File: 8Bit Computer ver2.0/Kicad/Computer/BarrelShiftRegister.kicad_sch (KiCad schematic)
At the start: 6 parts, among them IC75 SN74AHC157DR, IC76 SN74AHC157DR, IC77 SN74AHC157DR, IC78 SN74AHC157DR, IC79 SN74AHC157DR, IC80 SN74AHC157DR

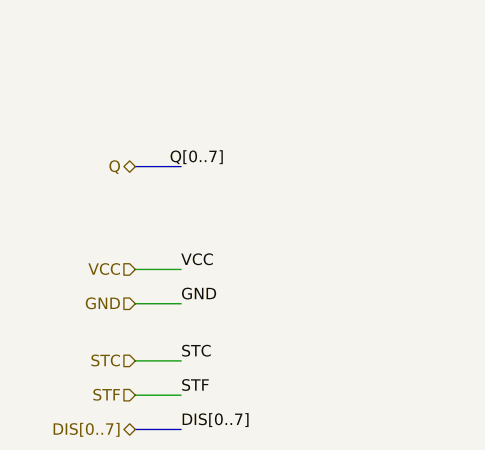
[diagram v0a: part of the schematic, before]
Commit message: partsList, Kicad
parts:
added faster Comparator 521
added 1CH XOR
added 8Bit and 16Bit Driver 245, 16245
->they need pullUp resistors for High-Z when power on
Kicad:
included SRAM CAD Model AS7C1024
included some CAD Models
added Register 1 0x20 and 0x21
finished Incrementor
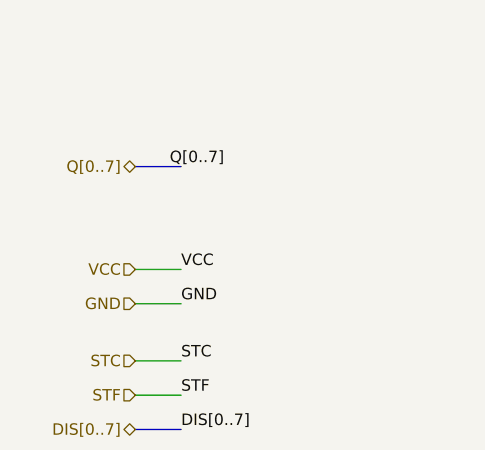
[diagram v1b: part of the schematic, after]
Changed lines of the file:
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@@
 		)
 	)
-	(hierarchical_label "Q"
+	(hierarchical_label "Q[0..7]"
 		(shape tri_state)
 		(at 39.37 43.18 180)

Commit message: Kicad
added Register 2(0x22 u 0x23) and 3(0x13 u 0x14)
added BarrelShiftRegister
added AdderSubstractor
added cmd Comparators to the bitwise and binary Logic
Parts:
- added IC115, IC116, IC117: SN74LVC1G08DBVR, Samacsys:SOT95P280X145-5N, symbol Samacsys:SN74LVC1G08DBVR
- added IC118: SN74AHC08DR, Samacsys:SOIC127P600X175-14N, symbol Samacsys:SN74AHC08DR
- added IC119: SN74ABT574ADWR, Samacsys:SOIC127P1030X265-20N, symbol Samacsys:SN74ABT574ADWR
- added IC120: SN74LVC1G32DBVR, Samacsys:SOT95P280X145-5N, symbol Samacsys:SN74LVC1G32DBVR
- added IC121: SN74AHC74DR, Samacsys:SOIC127P600X175-14N, symbol Samacsys:SN74AHC74DR
- added IC122: SN74LVC1G14DBVR, Samacsys:SOT95P280X145-5N, symbol Samacsys:SN74LVC1G14DBVR
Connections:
- net GND: now also IC115.3 (GND), IC116.3 (GND), IC117.3 (GND), IC118.7 (GND), IC119.10 (GND), IC120.3 (GND), IC121.7 (GND), IC122.3 (GND)
- net STC: now also IC115.2 (B), IC116.2 (B), IC117.2 (B), IC118.12 (4A), IC118.2 (1B), IC118.5 (2B), IC118.9 (3A)
- net VCC: now also IC115.5 (VCC), IC116.5 (VCC), IC117.5 (VCC), IC118.14 (VCC), IC119.20 (VCC), IC120.5 (VCC), IC121.1 (1~{CLR}), IC121.10 (2~{PRE}), IC121.11 (2CLK), IC121.12 (2D), IC121.13 (2~{CLR}), IC121.14 (VCC), IC121.4 (1~{PRE}), IC122.5 (VCC)
- net ~{CLK}: now also IC122.2 (A)
- net DIS1: now reaches IC77.1 (~{A}/B)
- net DIS1: now also IC78.1 (~{A}/B)
- net STC1Stage1: now reaches IC77.10 (3B)
- net STC1Stage1: now also IC117.4 (Y)
- net 1Stage7: now reaches IC77.11 (3A)
- net 1Stage7: now also IC76.9 (3Y), IC78.10 (3B)
- net 2Stage6: now reaches IC77.12 (4Y)
- net 2Stage6: now also IC80.14 (4A), IC80.3 (1B)
- net STC1Stage0: now reaches IC77.13 (4B)
- net STC1Stage0: now also IC116.4 (Y)
- net 1Stage6: now reaches IC77.14 (4A)
- net 1Stage6: now also IC76.12 (4Y), IC78.13 (4B)
- net 1Stage2: now reaches IC77.2 (1A)
- net 1Stage2: now also IC76.4 (1Y), IC78.3 (1B)
- net 1Stage4: now reaches IC77.3 (1B)
- net 1Stage4: now also IC75.12 (4Y), IC78.14 (4A)
- net 2Stage2: now reaches IC77.4 (1Y)
- net 2Stage2: now also IC80.2 (1A), IC118.13 (4B)
- net 1Stage3: now reaches IC77.5 (2A)
- net 1Stage3: now also IC76.7 (2Y), IC78.6 (2B)
- net 1Stage5: now reaches IC77.6 (2B)
- net 1Stage5: now also IC75.9 (3Y), IC78.11 (3A)
- net 2Stage3: now reaches IC77.7 (2Y)
- net 2Stage3: now also IC80.5 (2A), IC118.10 (3B)
- net 2Stage7: now reaches IC77.9 (3Y)
- net 2Stage7: now also IC80.11 (3A), IC80.6 (2B)
- net DIS0: now reaches IC76.1 (~{A}/B)
- net DIS0: now also IC75.1 (~{A}/B)
- net STCA0: now reaches IC76.10 (3B)
- net STCA0: now also IC115.4 (Y)
- net A7: now reaches IC76.11 (3A)
- net A7: now also IC76.13 (4B)
- net A6: now reaches IC76.14 (4A)
- net A6: now also IC75.10 (3B)
- net A2: now reaches IC76.2 (1A)
- net A2: now also IC75.6 (2B)
- net A3: now reaches IC76.3 (1B)
- net A3: now also IC76.5 (2A)
- net A4: now reaches IC76.6 (2B)
- net A4: now also IC75.14 (4A)
- net DIS2: now reaches IC79.1 (~{A}/B)
- net DIS2: now also IC80.1 (~{A}/B)
- net STC2Stage1: now reaches IC79.10 (3B)
- net STC2Stage1: now also IC118.6 (2Y)
- net 2Stage5: now reaches IC79.11 (3A)
- net 2Stage5: now also IC78.9 (3Y), IC79.6 (2B)
- net 3Stage4: now reaches IC79.12 (4Y)
- net 3Stage4: now also IC119.6 (5D)
- net STC2Stage0: now reaches IC79.13 (4B)
- net STC2Stage0: now also IC118.3 (1Y)
- net 2Stage4: now reaches IC79.14 (4A)
- net 2Stage4: now also IC78.12 (4Y), IC79.3 (1B)
- net 2Stage0: now reaches IC79.2 (1A)
- net 2Stage0: now also IC78.4 (1Y), IC118.1 (1A)
- net 3Stage0: now reaches IC79.4 (1Y)
- net 3Stage0: now also IC119.2 (1D)
- net 2Stage1: now reaches IC79.5 (2A)
- net 2Stage1: now also IC78.7 (2Y), IC118.4 (2A)
- net 3Stage1: now reaches IC79.7 (2Y)
- net 3Stage1: now also IC119.3 (2D)
- net 3Stage5: now reaches IC79.9 (3Y)
- net 3Stage5: now also IC119.7 (6D)
- net STC2Stage3: now reaches IC80.10 (3B)
- net STC2Stage3: now also IC118.8 (3Y)
- net 3Stage6: now reaches IC80.12 (4Y)
- net 3Stage6: now also IC119.8 (7D)
- net STC2Stage2: now reaches IC80.13 (4B)
- net STC2Stage2: now also IC118.11 (4Y)
- net 3Stage2: now reaches IC80.4 (1Y)
- net 3Stage2: now also IC119.4 (3D)
- net 3Stage3: now reaches IC80.7 (2Y)
- net 3Stage3: now also IC119.5 (4D)
- net 3Stage7: now reaches IC80.9 (3Y)
- net 3Stage7: now also IC119.9 (8D)
- net 1Stage0: now reaches IC78.2 (1A)
- net 1Stage0: now also IC75.4 (1Y), IC116.1 (A)
- net 1Stage1: now reaches IC78.5 (2A)
- net 1Stage1: now also IC75.7 (2Y), IC117.1 (A)
- net A5: now reaches IC75.11 (3A)
- net A5: now also IC75.13 (4B)
- net A0: now reaches IC75.2 (1A)
- net A0: now also IC115.1 (A)
- net A1: now reaches IC75.3 (1B)
- net A1: now also IC75.5 (2A)
- new net: IC119.1 (~{OE}), IC121.6 (1~{Q})
- new net: IC119.11 (CLK), IC121.5 (1Q)
- new net: IC121.3 (1CLK), IC122.4 (Y)
- new net: IC120.4 (Y), IC121.2 (1D)
- new net Q0: IC119.19 (1Q)
- new net Q1: IC119.18 (2Q)
- new net Q2: IC119.17 (3Q)
- new net Q3: IC119.16 (4Q)
- new net Q4: IC119.15 (5Q)
- new net Q5: IC119.14 (6Q)
- new net Q6: IC119.13 (7Q)
- new net Q7: IC119.12 (8Q)
- new net SFC: IC120.2 (B)
- new net SFT: IC120.1 (A)
- no-connect marks 0 -> 2
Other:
- moved on the sheet: IC75, IC76, IC77, IC78, IC79, IC80

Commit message: Kicad, parts
Parts:
added Leds
Kicad:
added Input Output
changed Q bus to DAT bus
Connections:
- net Q0 renamed DAT0
- net Q1 renamed DAT1
- net Q2 renamed DAT2
- net Q3 renamed DAT3
- net Q4 renamed DAT4
- net Q5 renamed DAT5
- net Q6 renamed DAT6
- net Q7 renamed DAT7
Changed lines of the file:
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@@
 		)
 	)
-	(label "Q6"
+	(label "DAT6"
 		(at 400.05 129.54 0)
 		(effects
@@
 		)
 	)
-	(label "Q5"
+	(label "DAT5"
 		(at 400.05 127 0)
 		(effects
@@
 		)
 	)
-	(label "Q7"
+	(label "DAT7"
 		(at 400.05 132.08 0)
 		(effects
@@
 		)
 	)
-	(label "Q4"
+	(label "DAT4"
 		(at 400.05 124.46 0)
 		(effects
@@
 		)
 	)
-	(label "Q3"
+	(label "DAT3"
 		(at 400.05 121.92 0)
 		(effects
@@
 		)
 	)
-	(label "Q[0..7]"
+	(label "DAT[0..7]"
 		(at 40.64 80.01 0)
 		(effects
@@
 		)
 	)
-	(label "Q0"
+	(label "DAT0"
 		(at 400.05 114.3 0)
 		(effects
@@
 		)
 	)
-	(label "Q2"
+	(label "DAT2"
 		(at 400.05 119.38 0)
 		(effects
@@
 		)
 	)
-	(label "Q[0..7]"
+	(label "DAT[0..7]"
 		(at 411.48 104.14 0)
 		(effects
@@
 		)
 	)
-	(label "Q1"
+	(label "DAT1"
 		(at 400.05 116.84 0)
 		(effects
@@
 		)
 	)
-	(hierarchical_label "Q[0..7]"
+	(hierarchical_label "DAT[0..7]"
 		(shape tri_state)
 		(at 36.83 80.01 180)

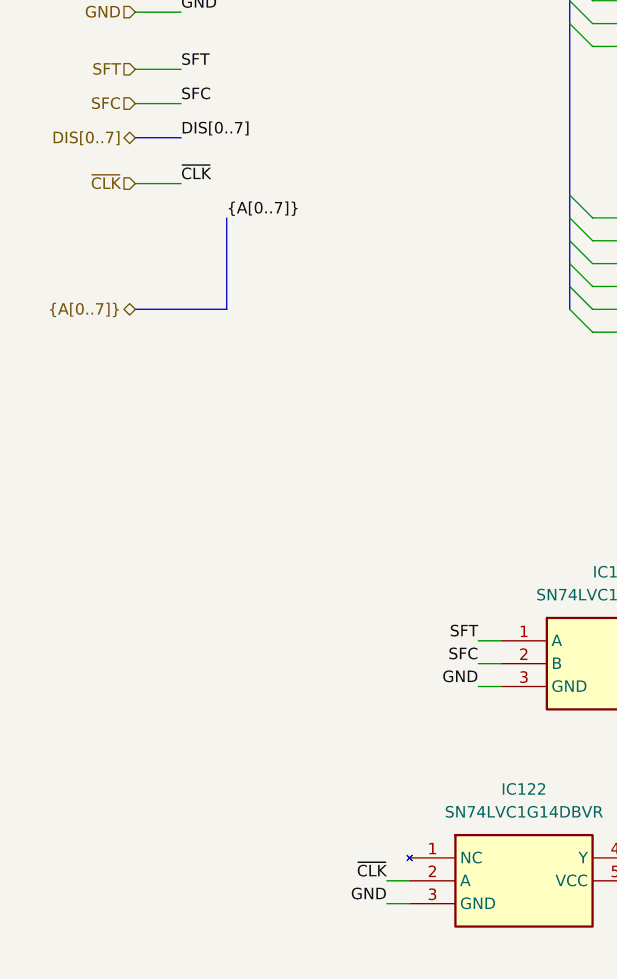
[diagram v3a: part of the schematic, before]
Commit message: Kicad, parts
parts:
added USB C PD Triggerboard
added Delay Chip for 90ns
added Push Button
Kicad:
added USB C PD Triggerboard
added rising edge detector via Delay and Xor for Accept Push Button
added VBUS net
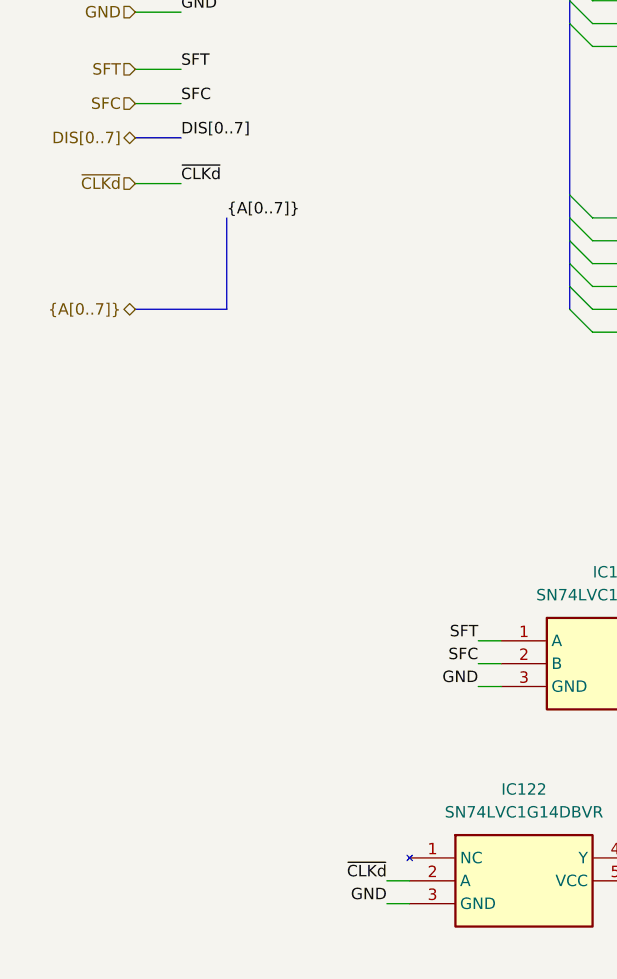
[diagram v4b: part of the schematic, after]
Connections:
- net ~{CLK} renamed ~{CLKd}
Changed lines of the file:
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@@
 		)
 	)
-	(label "~{CLK}"
+	(label "~{CLKd}"
 		(at 41.91 114.3 0)
 		(effects
@@
 		)
 	)
-	(label "~{CLK}"
+	(label "~{CLKd}"
 		(at 64.77 191.77 180)
 		(effects
@@
 		)
 	)
-	(hierarchical_label "~{CLK}"
+	(hierarchical_label "~{CLKd}"
 		(shape input)
 		(at 36.83 114.3 180)

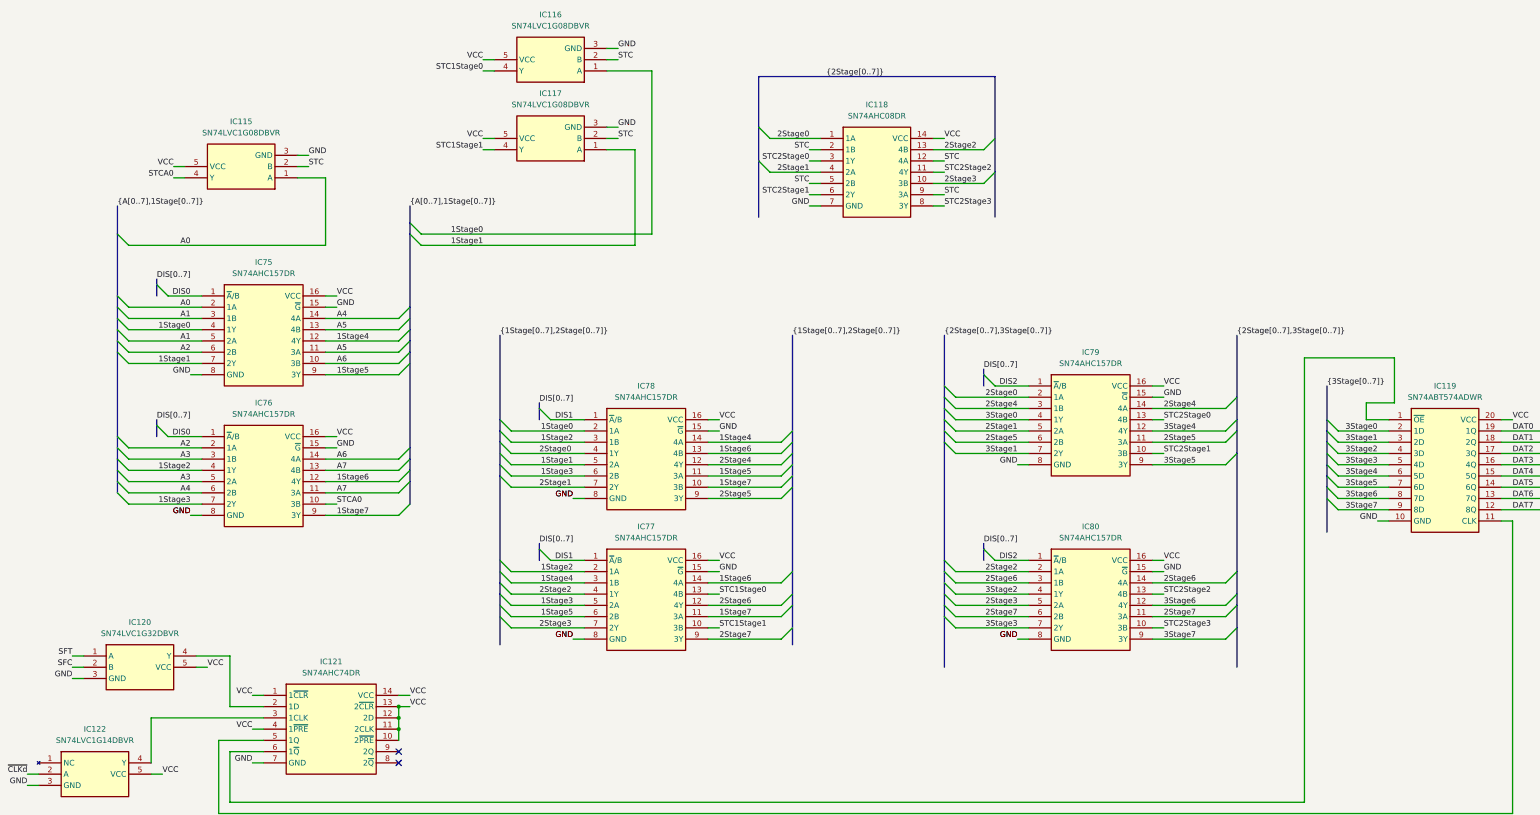
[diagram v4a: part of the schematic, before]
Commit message: Kicad SCH/PCB
Kicad SCH/PCB:
changed the References in SCH
began with INOUTPUT module nearly done
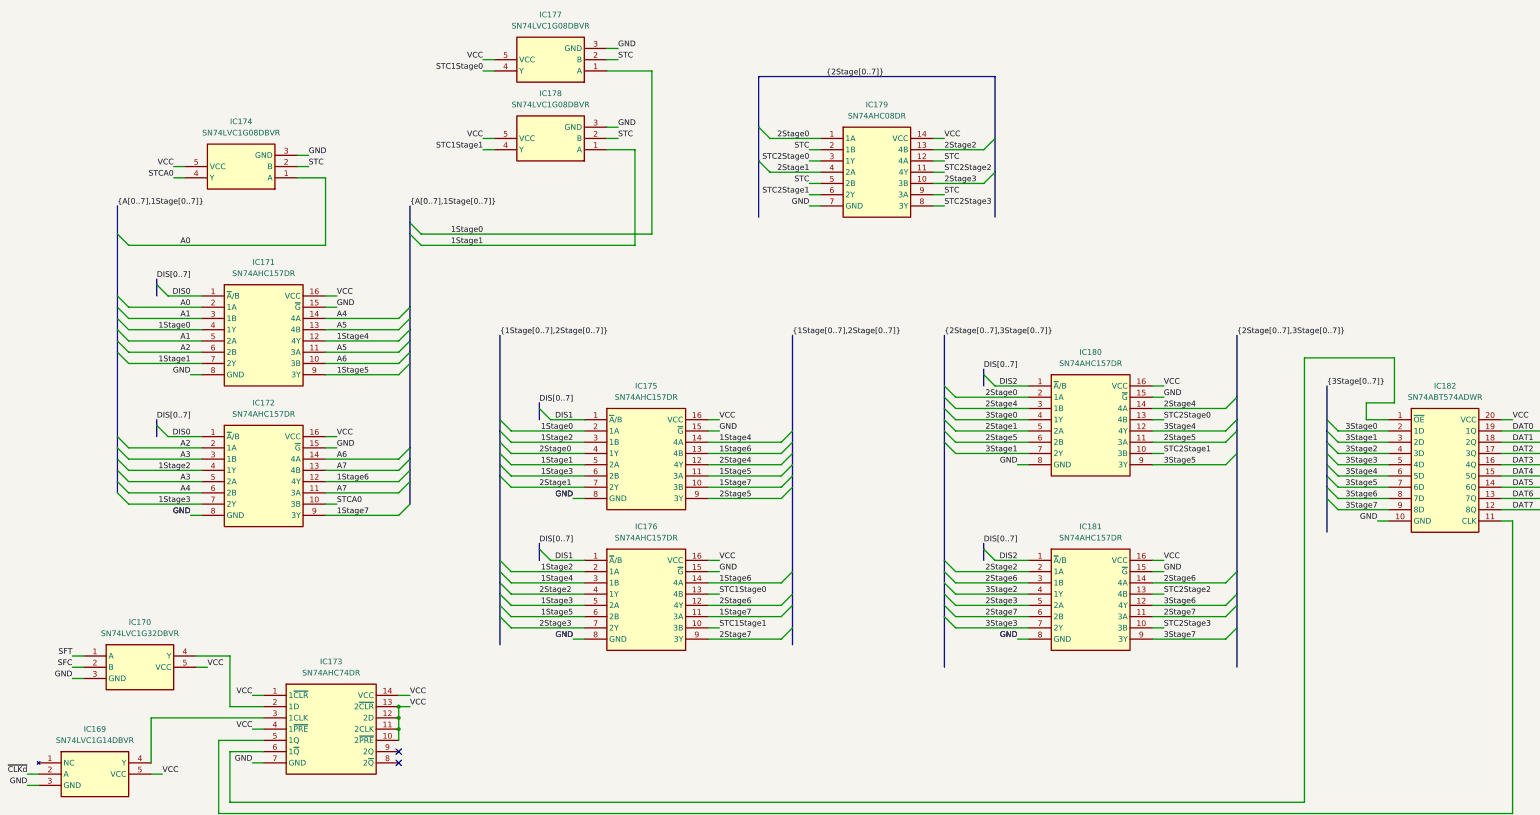
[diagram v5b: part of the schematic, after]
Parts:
- renumbered IC122 to IC169, IC120 to IC170, IC75 to IC171, IC76 to IC172, IC121 to IC173, IC115 to IC174, IC78 to IC175, IC77 to IC176, IC116 to IC177, IC117 to IC178, IC118 to IC179, IC79 to IC180, IC80 to IC181, IC119 to IC182
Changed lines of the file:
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@@
 		(dnp no)
 		(fields_autoplaced yes)
-		(property "Reference" "IC116"
+		(property "Reference" "IC177"
 			(at 182.88 20.32 0)
 			(effects
@@
 			(project "Computer"
 				(path "/1196a00e-6878-4d6d-82b7-9e052dfe7c14/c4d8b530-1c6d-45af-88d2-7dc1d4321a34/94505ca6-4c2b-4b0f-b160-ac9607e51728"
-					(reference "IC116")
+					(reference "IC177")
 					(unit 1)
 				)
@@
 		(dnp no)
 		(fields_autoplaced yes)
-		(property "Reference" "IC77"
+		(property "Reference" "IC176"
 			(at 204.47 135.89 0)
 			(effects
@@
 			(project "Computer"
 				(path "/1196a00e-6878-4d6d-82b7-9e052dfe7c14/c4d8b530-1c6d-45af-88d2-7dc1d4321a34/94505ca6-4c2b-4b0f-b160-ac9607e51728"
-					(reference "IC77")
+					(reference "IC176")
 					(unit 1)
 				)
@@
 		(dnp no)
 		(fields_autoplaced yes)
-		(property "Reference" "IC76"
+		(property "Reference" "IC172"
 			(at 118.11 107.95 0)
 			(effects
@@
 			(project "Computer"
 				(path "/1196a00e-6878-4d6d-82b7-9e052dfe7c14/c4d8b530-1c6d-45af-88d2-7dc1d4321a34/94505ca6-4c2b-4b0f-b160-ac9607e51728"
-					(reference "IC76")
+					(reference "IC172")
 					(unit 1)
 				)
@@
 		(dnp no)
 		(fields_autoplaced yes)
-		(property "Reference" "IC79"
+		(property "Reference" "IC180"
 			(at 304.8 96.52 0)
 			(effects
@@
 			(project "Computer"
 				(path "/1196a00e-6878-4d6d-82b7-9e052dfe7c14/c4d8b530-1c6d-45af-88d2-7dc1d4321a34/94505ca6-4c2b-4b0f-b160-ac9607e51728"
-					(reference "IC79")
+					(reference "IC180")
 					(unit 1)
 				)
@@
 		(dnp no)
 		(fields_autoplaced yes)
-		(property "Reference" "IC80"
+		(property "Reference" "IC181"
 			(at 304.8 135.89 0)
 			(effects
@@
 			(project "Computer"
 				(path "/1196a00e-6878-4d6d-82b7-9e052dfe7c14/c4d8b530-1c6d-45af-88d2-7dc1d4321a34/94505ca6-4c2b-4b0f-b160-ac9607e51728"
-					(reference "IC80")
+					(reference "IC181")
 					(unit 1)
 				)
@@
 		(dnp no)
 		(fields_autoplaced yes)
-		(property "Reference" "IC119"
+		(property "Reference" "IC182"
 			(at 384.81 104.14 0)
 			(effects
@@
 			(project ""
 				(path "/1196a00e-6878-4d6d-82b7-9e052dfe7c14/c4d8b530-1c6d-45af-88d2-7dc1d4321a34/94505ca6-4c2b-4b0f-b160-ac9607e51728"
-					(reference "IC119")
+					(reference "IC182")
 					(unit 1)
 				)
@@
 		(dnp no)
 		(fields_autoplaced yes)
-		(property "Reference" "IC117"
+		(property "Reference" "IC178"
 			(at 182.88 38.1 0)
 			(effects
@@
 			(project "Computer"
 				(path "/1196a00e-6878-4d6d-82b7-9e052dfe7c14/c4d8b530-1c6d-45af-88d2-7dc1d4321a34/94505ca6-4c2b-4b0f-b160-ac9607e51728"
-					(reference "IC117")
+					(reference "IC178")
 					(unit 1)
 				)
@@
 		(dnp no)
 		(fields_autoplaced yes)
-		(property "Reference" "IC118"
+		(property "Reference" "IC179"
 			(at 256.54 40.64 0)
 			(effects
@@
 			(project ""
 				(path "/1196a00e-6878-4d6d-82b7-9e052dfe7c14/c4d8b530-1c6d-45af-88d2-7dc1d4321a34/94505ca6-4c2b-4b0f-b160-ac9607e51728"
-					(reference "IC118")
+					(reference "IC179")
 					(unit 1)
 				)
@@
 		(dnp no)
 		(fields_autoplaced yes)
-		(property "Reference" "IC122"
+		(property "Reference" "IC169"
 			(at 80.01 181.61 0)
 			(effects
@@
 			(project ""
 				(path "/1196a00e-6878-4d6d-82b7-9e052dfe7c14/c4d8b530-1c6d-45af-88d2-7dc1d4321a34/94505ca6-4c2b-4b0f-b160-ac9607e51728"
-					(reference "IC122")
+					(reference "IC169")
 					(unit 1)
 				)
@@
 		(dnp no)
 		(fields_autoplaced yes)
-		(property "Reference" "IC115"
+		(property "Reference" "IC174"
 			(at 113.03 44.45 0)
 			(effects
@@
 			(project ""
 				(path "/1196a00e-6878-4d6d-82b7-9e052dfe7c14/c4d8b530-1c6d-45af-88d2-7dc1d4321a34/94505ca6-4c2b-4b0f-b160-ac9607e51728"
-					(reference "IC115")
+					(reference "IC174")
 					(unit 1)
 				)
@@
 		(dnp no)
 		(fields_autoplaced yes)
-		(property "Reference" "IC120"
+		(property "Reference" "IC170"
 			(at 90.17 157.48 0)
 			(effects
@@
 			(project ""
 				(path "/1196a00e-6878-4d6d-82b7-9e052dfe7c14/c4d8b530-1c6d-45af-88d2-7dc1d4321a34/94505ca6-4c2b-4b0f-b160-ac9607e51728"
-					(reference "IC120")
+					(reference "IC170")
 					(unit 1)
 				)
@@
 		(dnp no)
 		(fields_autoplaced yes)
-		(property "Reference" "IC121"
+		(property "Reference" "IC173"
 			(at 133.35 166.37 0)
 			(effects
@@
 			(project ""
 				(path "/1196a00e-6878-4d6d-82b7-9e052dfe7c14/c4d8b530-1c6d-45af-88d2-7dc1d4321a34/94505ca6-4c2b-4b0f-b160-ac9607e51728"
-					(reference "IC121")
+					(reference "IC173")
 					(unit 1)
 				)
@@
 		(dnp no)
 		(fields_autoplaced yes)
-		(property "Reference" "IC78"
+		(property "Reference" "IC175"
 			(at 204.47 104.14 0)
 			(effects
@@
 			(project "Computer"
 				(path "/1196a00e-6878-4d6d-82b7-9e052dfe7c14/c4d8b530-1c6d-45af-88d2-7dc1d4321a34/94505ca6-4c2b-4b0f-b160-ac9607e51728"
-					(reference "IC78")
+					(reference "IC175")
 					(unit 1)
 				)
@@
 		(dnp no)
 		(fields_autoplaced yes)
-		(property "Reference" "IC75"
+		(property "Reference" "IC171"
 			(at 118.11 76.2 0)
 			(effects
@@
 			(project ""
 				(path "/1196a00e-6878-4d6d-82b7-9e052dfe7c14/c4d8b530-1c6d-45af-88d2-7dc1d4321a34/94505ca6-4c2b-4b0f-b160-ac9607e51728"
-					(reference "IC75")
+					(reference "IC171")
 					(unit 1)
 				)
